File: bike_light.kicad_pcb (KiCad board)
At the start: 2 copper layers, 181 parts, among them P1 CONN_6_RA_MALE, P2 CONN_6_RA_FEMALE, P3 CONN_6_RA_MALE, P4 CONN_6_RA_MALE, P5 CONN_6_MALE_FRONT, P6 CONN_6_MALE_BACK, Q1 AON7611, Q4 DMN65D8L, Q5 DMN65D8L, Q6 DMN65D8L, Q7 DMN65D8L, Q8 DMN65D8L, Q9 DMN65D8L, U1 TEST_PT, U10 TEST_PT, U11 TEST_PT, U12 TEST_PT, U13 TEST_PT, U14 TEST_PT, U15 TEST_PT, U16 TEST_PT, U17 TEST_PT, U18 TEST_PT, U19 TEST_PT, U2 TEST_PT, U20 MCP6L02, U21 74LVC2G06, U22 TPS3700, U23 NC7WZ08, U3 TEST_PT, U30 MSP430G2203IPW28, U31 BH1620FVC, U32 MMA7660FC, U33 AT42QT1011, U34 TOUCHPAD, U35 AT42QT1011, U36 TOUCHPAD, U37 AT42QT1011, U38 TOUCHPAD, U39 TLC59108IPWR, U4 TEST_PT, U40 TLC59108IPWR, U41 TLC59108IPWR, U42 TPS62090, U43 LM3668, U44 CONN_JTAG_14_2_wire, U45 CP2110, U46 ESDR0502N, U47 CONN_USB, U48 BQ24190, U5 TEST_PT, U6 TEST_PT, U7 TEST_PT, U8 TEST_PT, U9 TEST_PT

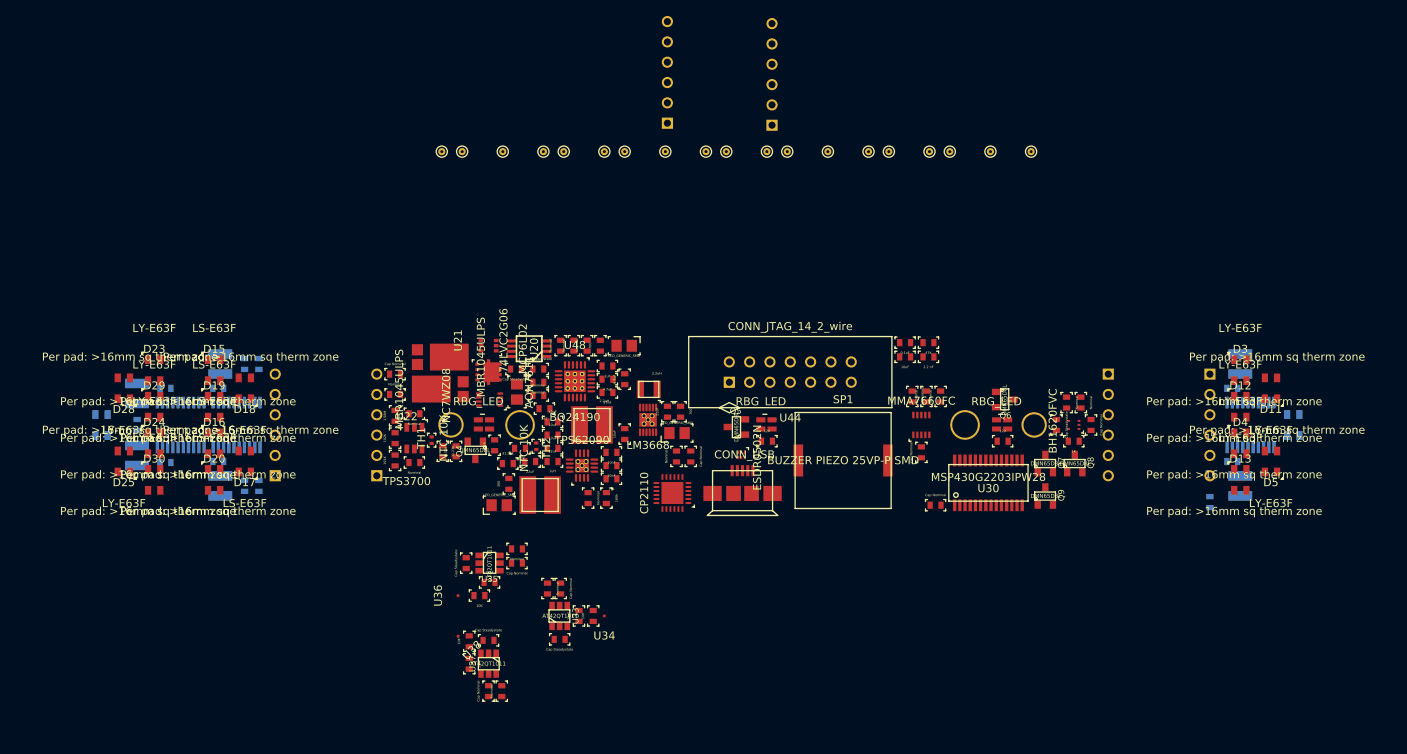
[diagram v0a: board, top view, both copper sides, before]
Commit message: revised connections between boards
now right and left will be identical and easy to assemble.
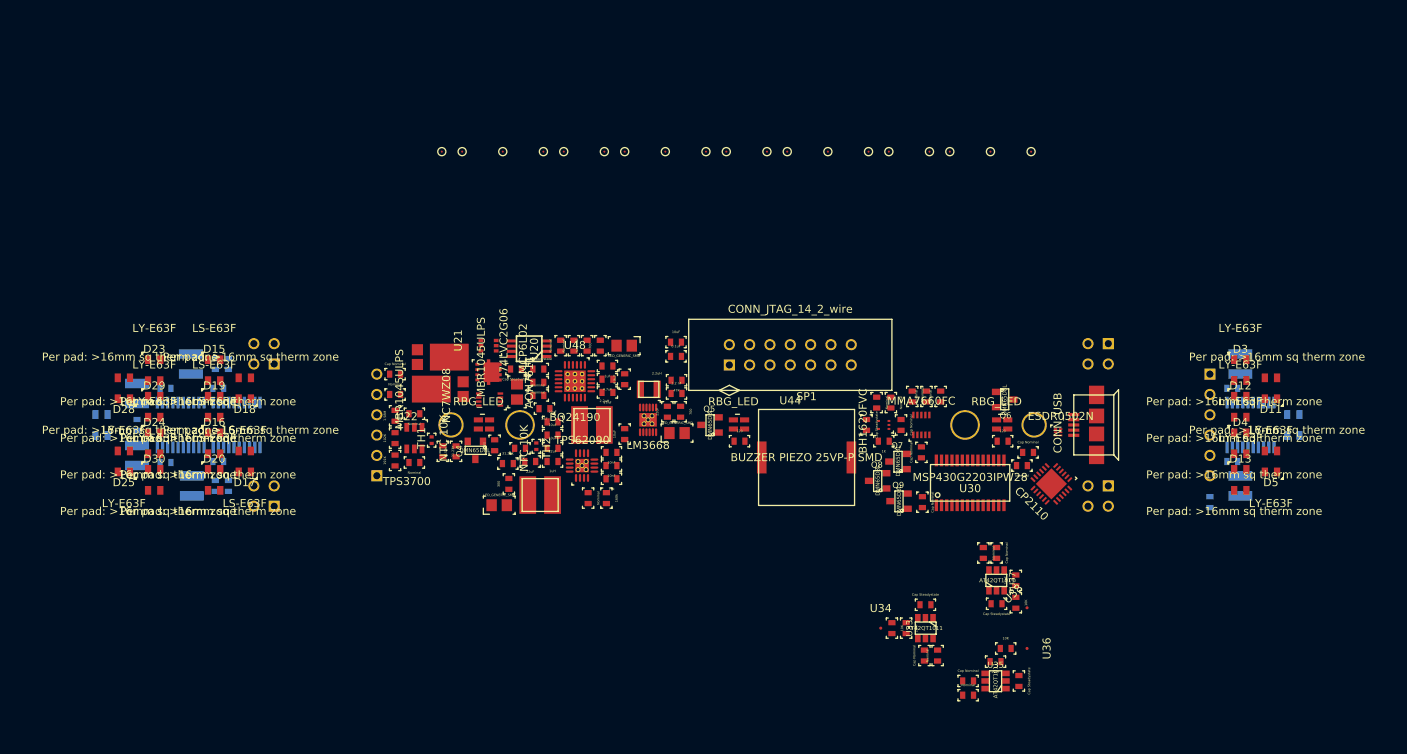
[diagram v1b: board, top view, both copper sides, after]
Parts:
- P2: value CONN_6_RA_FEMALE -> CONN_2x2_MALE_RA; footprint CONN_6_FEMALE -> CONN_2x2_MALE_RA
- P3: value CONN_6_RA_MALE -> CONN_2x2_MALE_RA; footprint CONN_6_MALE_RA -> CONN_2x2_MALE_RA
- P4: value CONN_6_RA_MALE -> CONN_2x2_FEMALE_BACK; footprint CONN_6_MALE_RA -> CONN_2x2
- P5: value CONN_6_MALE_FRONT -> CONN_6_FEMALE_FRONT
- P6: value CONN_6_MALE_BACK -> CONN_2x2_FEMALE_BACK; footprint CONN_6_FEMALE -> CONN_2x2
- moved P2 78.4 mm to (95.6, 93.7)
- moved U36 71.4 mm to (189.7, 111.5), turned to 90 degrees
- moved U38 71.2 mm to (189.7, 106.4), turned to 225 degrees
- moved C12 70.6 mm to (188.7, 115.6), turned to 90 degrees
- moved C14 69.1 mm to (188.3, 103.0), turned to 270 degrees
- moved R26 68.5 mm to (188.3, 105.8), turned to 90 degrees
- moved R24 66.1 mm to (187.1, 111.5), turned to 180 degrees
- moved C16 65.8 mm to (185.9, 99.6), turned to 90 degrees
- moved U35 64.9 mm to (185.8, 115.6), turned to 90 degrees
- moved U37 64.3 mm to (185.9, 103.0), turned to 0 degrees
- moved C11 64.0 mm to (185.8, 113.2), turned to 0 degrees
- moved C15 63.7 mm to (185.9, 105.9), turned to 0 degrees
- moved R27 62.6 mm to (184.3, 99.6), turned to 90 degrees
- moved P4 61.6 mm to (199.9, 73.4), turned to 270 degrees
- moved R25 59.3 mm to (182.4, 117.3), turned to 180 degrees
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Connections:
- P2 pad 3: /battery_charger/SCL -> /output_signal_brake_2/brake_leds/+2.5V
- P2 pad 4: /battery_charger/SDA -> /output_signal_brake_2/~RESET
- P3 pad 1: +3.3V -> AGND
- P3 pad 2: /output_signal_brake_2/brake_leds/+2.5V -> /battery_charger/SCL
- P3 pad 3: /battery_charger/SCL -> /battery_charger/SDA
- P3 pad 4: /battery_charger/SDA -> AGND
- P4 pad 3: /battery_charger/SCL -> /output_signal_brake_2/brake_leds/+2.5V
- P4 pad 4: /battery_charger/SDA -> /output_signal_brake_2/~RESET
- P6 pad 1: +3.3V -> AGND
- P6 pad 2: /output_signal_brake_2/brake_leds/+2.5V -> /battery_charger/SCL
- P6 pad 3: /battery_charger/SCL -> /battery_charger/SDA
- P6 pad 4: /battery_charger/SDA -> AGND

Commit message: began routing!!!!!
:D
gonna try the autorouter after important traces.
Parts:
- added P10: CONN_2, CONN_2x1, F.Cu at (180.7, 101.9)
- added P11: CONN_2, CONN_2x1, F.Cu at (180.7, 99.3)
- added P12: CONN_2, CONN_2x1_FEMALE, F.Cu at (108.7, 73.4)
- added P13: CONN_2, CONN_2x1_FEMALE, F.Cu at (108.7, 93.7)
- added P14: CONN_2, CONN_2x1_FEMALE, F.Cu at (180.7, 73.9)
- added P15: CONN_2, CONN_2x1_FEMALE, F.Cu at (180.7, 76.5)
- added P16: CONN_2, CONN_2x1_FEMALE, F.Cu at (180.7, 79.0)
- added P7: CONN_2, CONN_2x1, F.Cu at (108.7, 98.8)
- added P8: CONN_2, CONN_2x1, F.Cu at (108.7, 119.1)
- added P9: CONN_2, CONN_2x1, F.Cu at (180.7, 104.4)
- U1, U10, U11, U12, U13, U14, U15, U16, U17, U18, U19, U2, U3, U4, U5, U6, U7, U8, U9: moved to B.Cu
- moved R27 1.53 mm to (185.7, 98.9)
- moved C16 1.53 mm to (187.3, 98.9)
- moved C14 1.37 mm to (188.8, 101.7)
- moved R26 1.37 mm to (188.8, 104.5)
- moved R20 1.02 mm to (177.9, 80.0)
- moved R21 0.89 mm to (176.3, 80.0)
- moved C6 0.76 mm to (174.6, 80.0)
- moved U37 0.72 mm to (186.4, 102.5)
- moved U1 0.63 mm to (136.9, 48.8)
- moved U10 0.63 mm to (149.6, 48.8)
- moved U11 0.63 mm to (152.1, 48.8)
- moved U12 0.63 mm to (144.5, 48.8)
- moved U13 0.63 mm to (157.2, 48.8)
- moved U14 0.63 mm to (131.8, 48.8)
- moved U15 0.63 mm to (164.8, 48.8)
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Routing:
- net /battery_pack/battery_module_1/~OV: track 0.00 -> 16.1 mm, vias 0 -> 2
- net /battery_pack/battery_module_1/~UV: track 0.00 -> 12.8 mm, vias 0 -> 2
- net N-00000185: track 0.00 -> 9.13 mm, vias 0 -> 2
- net AGND: track 0.00 -> 9.09 mm
- net /battery_pack/battery_module_1/~CHG: track 0.00 -> 7.21 mm, vias 0 -> 2
- net N-00000196: track 0.00 -> 5.63 mm
- net /battery_pack/battery_module_1/PMOS_CTRL: track 0.00 -> 5.53 mm
- net N-00000101: track 0.00 -> 4.54 mm
- net +3.3V: track 0.00 -> 4.02 mm
- net /battery_pack/battery_module_1/NMOS_CTRL: track 0.00 -> 3.97 mm
- net N-00000191: track 0.00 -> 2.95 mm
- net N-00000190: track 0.00 -> 2.95 mm
- net /battery_pack/battery_module_1/V_BATT: track 0.00 -> 2.62 mm
- net /battery_pack/battery_module_1/CHG: track 0.00 -> 1.99 mm
- net /output_signal_brake_2/~RESET: track 0.00 -> 1.61 mm
- added copper zone on F.Cu, net /battery_pack/battery_module_1/V_BATT
- added copper zone on B.Cu, net /output_signal_brake_2/brake_leds/+2.5V
- added copper zone on F.Cu, net /output_signal_brake_2/brake_leds/+2.5V
- added copper zone on B.Cu, net /output_signal_brake_2/brake_leds/CATHODE_7
- added copper zone on B.Cu, net /output_signal_brake_2/brake_leds/CATHODE_8
- added copper zone on B.Cu, net /output_signal_brake_2/signal_leds_back/CATHODE_8
- added copper zone on B.Cu, net AGND
- added copper zone on F.Cu, net N-00000192
- added copper zone on F.Cu, net N-00000195
- added copper zone on F.Cu, net N-00000196
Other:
- board outline added: 25.4 x 22.9 mm
- copper layers 2 -> 4
- net class Default: clearance 0.254 -> 0.1524; via_dia 0.889 -> 0.762; via_drill 0.635 -> 0.381
- rule trace_clearance: 0.254 -> 0.1524
- rule trace_min: 0.254 -> 0.1524
- rule via_min_drill: 0.508 -> 0.381
- rule via_min_size: 0.889 -> 0.762

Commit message: did 1 trace...
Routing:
- net /battery_pack/battery_module_1/V_BATT: track 2.62 -> 5.29 mm
- net +3.3V: track 4.02 -> 5.20 mm, vias 0 -> 1

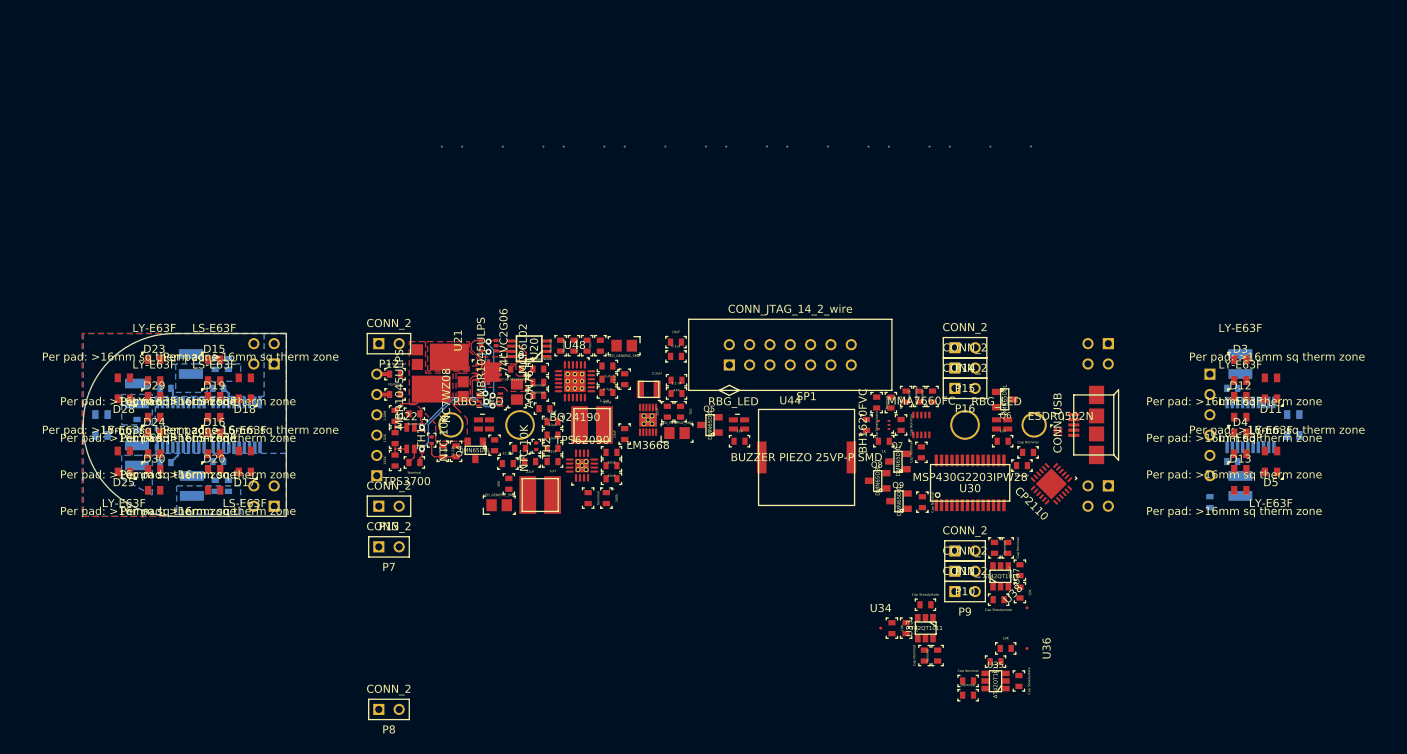
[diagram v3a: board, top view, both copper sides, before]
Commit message: routed 70% of board, made adjustments to schematics as necessary
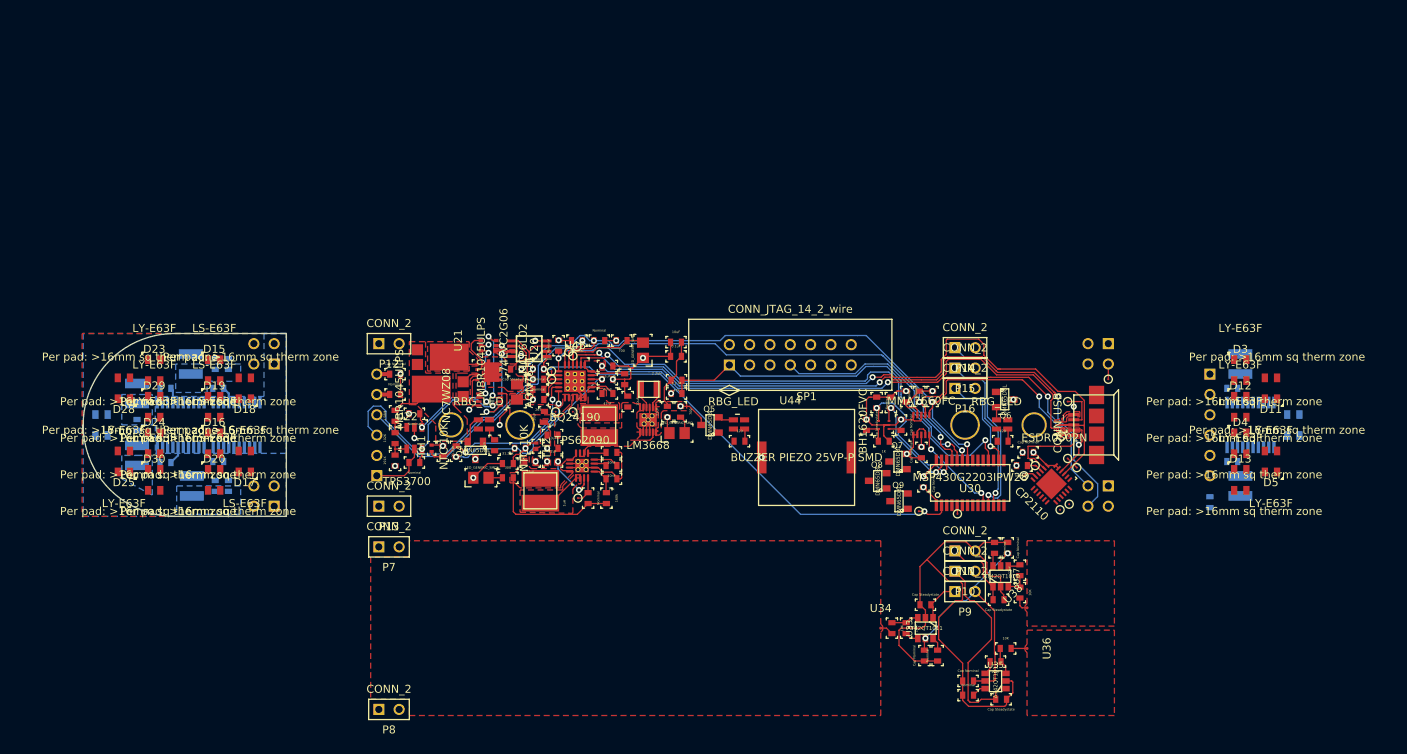
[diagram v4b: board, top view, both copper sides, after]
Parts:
- U1, U10, U11, U12, U13, U14, U15, U16, U17, U18, U19, U2, U3, U4, U5, U6, U7, U8, U9: moved to F.Cu
- moved U14 77.4 mm to (195.0, 93.5)
- moved U12 67.1 mm to (193.9, 94.2)
- moved U7 63.7 mm to (130.8, 81.9)
- moved U11 54.2 mm to (181.0, 94.7)
- moved U13 52.1 mm to (190.8, 88.6)
- moved U6 49.6 mm to (199.9, 77.9)
- moved U15 47.9 mm to (189.4, 89.9)
- moved U3 47.7 mm to (176.2, 94.4)
- moved U17 44.2 mm to (196.0, 88.9)
- moved U5 44.2 mm to (133.6, 92.7)
- moved U18 43.5 mm to (194.1, 85.0)
- moved U16 41.7 mm to (194.8, 87.8)
- moved U19 38.9 mm to (194.8, 80.6)
- moved U10 34.9 mm to (130.3, 77.9)
- moved U1 33.4 mm to (133.0, 81.9)
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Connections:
- U46 pad 1: AGND -> /battery_charger/USB_D-
- U46 pad 3: /battery_charger/USB_D- -> AGND
- U46 pad 4: /battery_charger/USB_D- -> AGND
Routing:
- net AGND: track 9.09 -> 172.6 mm, vias 0 -> 25
- net /battery_charger/SCL: track 0.00 -> 136.6 mm, vias 0 -> 4
- net /battery_charger/SDA: track 0.00 -> 134.6 mm, vias 0 -> 4
- net /battery_charger/USB_D+: track 0.00 -> 88.4 mm, vias 0 -> 2
- net /battery_charger/USB_D-: track 0.00 -> 84.6 mm, vias 0 -> 4
- net /battery_charger/USB_5V: track 0.00 -> 80.6 mm, vias 0 -> 2
- net +3.3V: track 5.20 -> 83.5 mm, vias 1 -> 18
- net /battery_charger/INT: track 0.00 -> 68.5 mm, vias 0 -> 2
- net /micro_proc/ADC_BATT: track 0.00 -> 61.8 mm, vias 0 -> 2
- net /micro_proc/TOUCH_2: track 0.00 -> 46.3 mm, vias 0 -> 1
- net /interface_JTAG_2_wire/SBWTDIO: track 0.00 -> 45.4 mm, vias 0 -> 1
- net /micro_proc/TOUCH_1: track 0.00 -> 30.7 mm, vias 0 -> 1
- net /interface_JTAG_2_wire/SBWTCK: track 0.00 -> 28.9 mm, vias 0 -> 1
- net N-00000103: track 0.00 -> 24.8 mm, vias 0 -> 3
- net /micro_proc/TOUCH_3: track 0.00 -> 22.0 mm, vias 0 -> 1
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- added copper zone on F.Cu, net +3.3V
- added copper zone on Inner2.Cu, net +3.3V
- added copper zone on F.Cu, net /battery_charger/BATT
- added copper zone on F.Cu, net /battery_charger/USB_5V
- added copper zone on F.Cu, net /battery_charger/USB_D-
- added copper zone on F.Cu, net /battery_pack/battery_module_1/CHG
- added copper zone on F.Cu, net /output_signal_brake_2/BATT_IN
- added copper zone on F.Cu, net AGND
- added copper zone on Inner1.Cu, net AGND
- added copper zone on F.Cu, net N-00000172
- added copper zone on F.Cu, net N-0000078
- added copper zone on F.Cu, net N-0000081
- added copper zone on F.Cu, net N-0000087
- added copper zone on F.Cu, net N-0000099

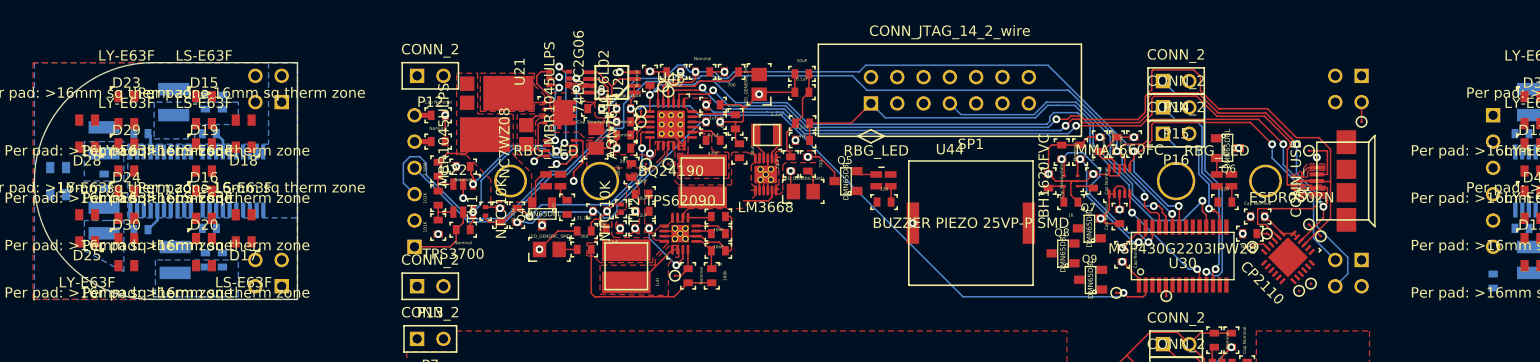
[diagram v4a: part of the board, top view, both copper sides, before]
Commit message: routed the back light module
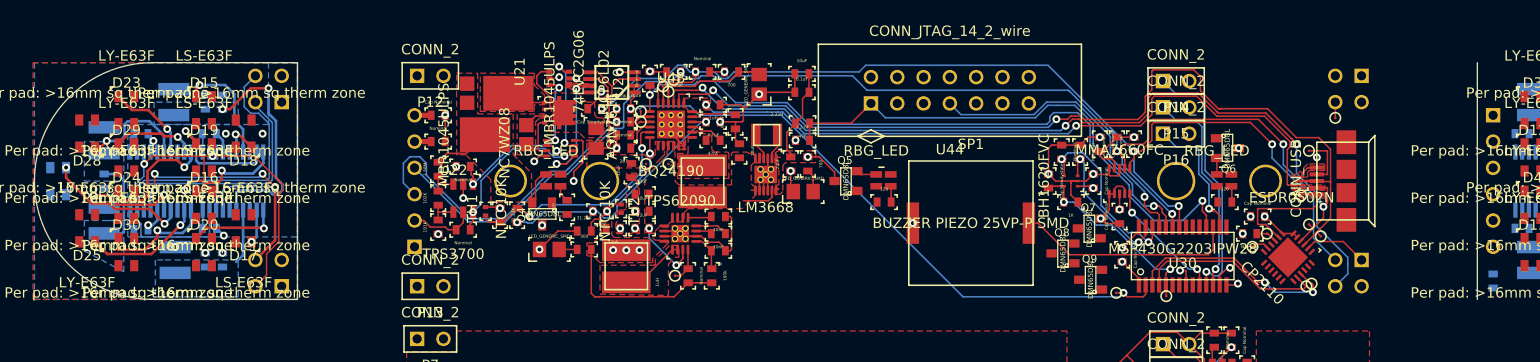
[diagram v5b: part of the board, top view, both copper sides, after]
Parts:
- moved U6 2.57 mm to (197.4, 77.5)
- moved U12 0.83 mm to (194.6, 93.7)
- moved U14 0.06 mm to (195.1, 93.5)
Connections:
- P2 pad 1: +3.3V -> /output_signal_brake_2/brake_leds/+2.5V
- P2 pad 2: /output_signal_brake_2/brake_leds/+2.5V -> +3.3V
- P2 pad 3: /output_signal_brake_2/brake_leds/+2.5V -> /output_signal_brake_2/~RESET
- P2 pad 4: /output_signal_brake_2/~RESET -> /output_signal_brake_2/brake_leds/+2.5V
- P4 pad 1: +3.3V -> /output_signal_brake_2/brake_leds/+2.5V
- P4 pad 2: /output_signal_brake_2/brake_leds/+2.5V -> +3.3V
- P4 pad 3: /output_signal_brake_2/brake_leds/+2.5V -> /output_signal_brake_2/~RESET
- P4 pad 4: /output_signal_brake_2/~RESET -> /output_signal_brake_2/brake_leds/+2.5V
- P5 pad 1: +3.3V -> /output_signal_brake_2/brake_leds/+2.5V
- P5 pad 2: /output_signal_brake_2/brake_leds/+2.5V -> +3.3V
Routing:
- net +3.3V: track 83.5 -> 125.8 mm, vias 18 -> 22
- net /battery_charger/SDA: track 134.6 -> 173.5 mm
- net /output_signal_brake_2/~RESET: track 3.51 -> 34.2 mm, vias 0 -> 4
- net /battery_charger/SCL: track 136.6 -> 162.3 mm
- net /output_signal_brake_2/brake_leds/CATHODE_8: track 0.00 -> 22.2 mm, vias 0 -> 2
- net /micro_proc/SPEAKER: track 0.00 -> 21.4 mm
- net /micro_proc/UART_RX: track 0.00 -> 21.0 mm, vias 0 -> 2
- net /output_signal_brake_2/signal_leds_back/CATHODE_8: track 0.00 -> 21.0 mm, vias 0 -> 2
- net /interface_usb/UART_RX: track 0.00 -> 18.5 mm
- net /micro_proc/ADC_LIGHT: track 4.22 -> 18.9 mm, vias 0 -> 2
- net /output_signal_brake_2/signal_leds_back/CATHODE_7: track 0.00 -> 13.9 mm, vias 0 -> 2
- net /output_signal_brake_2/signal_leds_back/CATHODE_4: track 0.00 -> 12.3 mm, vias 0 -> 1
- net /output_signal_brake_2/brake_leds/CATHODE_3: track 0.00 -> 11.9 mm, vias 0 -> 1
- net /output_signal_brake_2/signal_leds_back/CATHODE_6: track 0.00 -> 11.5 mm, vias 0 -> 1
- net /output_signal_brake_2/signal_leds_back/CATHODE_5: track 0.00 -> 11.4 mm, vias 0 -> 1
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- added copper zone on Inner_3.3V_2.5V.Cu, net +3.3V
- added copper zone on Inner_3.3V_2.5V.Cu, net /output_signal_brake_2/brake_leds/+2.5V
- added copper zone on Inner_GND.Cu, net AGND
- removed copper zone on Inner2.Cu, net +3.3V
- removed copper zone on Inner1.Cu, net AGND
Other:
- board size 25.4 x 22.9 mm -> 139.3 x 22.9 mm
